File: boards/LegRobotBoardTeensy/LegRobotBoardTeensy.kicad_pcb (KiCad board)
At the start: 2 copper layers, 142.8 x 110.9 mm, 164 parts, among them J1 IDC, J10 IDC, J11 IDC, J12 IDC, J13 IDC, J14 IDC, J15 IDC, J16 IDC, J2 B3B-XH-A, J3 B3B-XH-A, J4 B3B-XH-A, J5 B3B-XH-A, J6 IDC, J7 IDC, J8 IDC, J9 IDC, Q1 AO3400A, Q10 AO3400A, Q11 AO3400A, Q12 AO3400A, Q13 AO3400A, Q14 AO3400A, Q15 AO3400A, Q16 AO3400A, Q17 AO3400A, Q18 AO3400A, Q19 AO3400A, Q2 AO3400A, Q20 AO3400A, Q21 AO3400A, Q22 AO3400A, Q23 AO3400A, Q24 AO3400A, Q3 AO3400A, Q4 AO3400A, Q5 AO3400A, Q6 AO3400A, Q7 AO3400A, Q8 AO3400A, Q9 AO3400A, U1 Teensy4.0, U2 TLC555CDR, U3 SN74HC08DR, U4 SN74HC08DR, U5 PCA9685PW_118, U6 SN74HC08DR, U7 SN74HC08DR, U8 BNO055

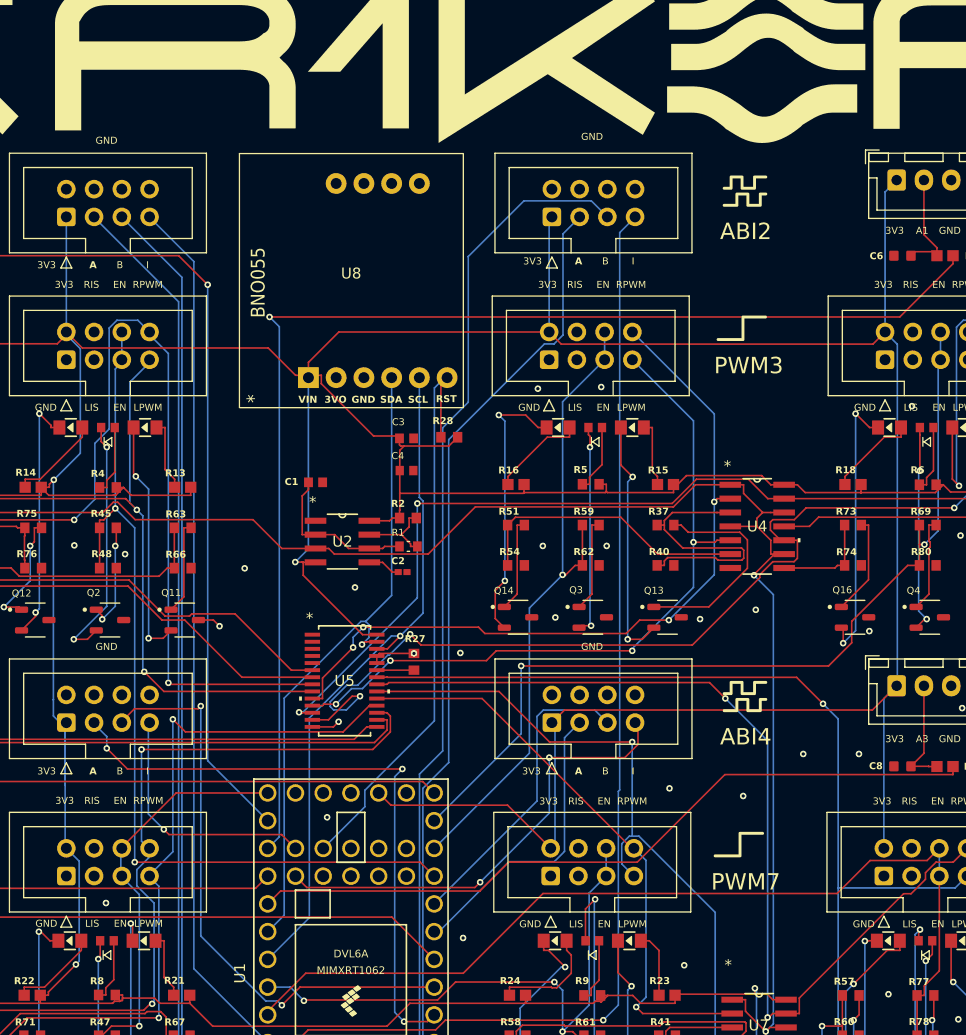
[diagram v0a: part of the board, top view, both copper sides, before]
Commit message: Re-routing leg board after rotating IMU
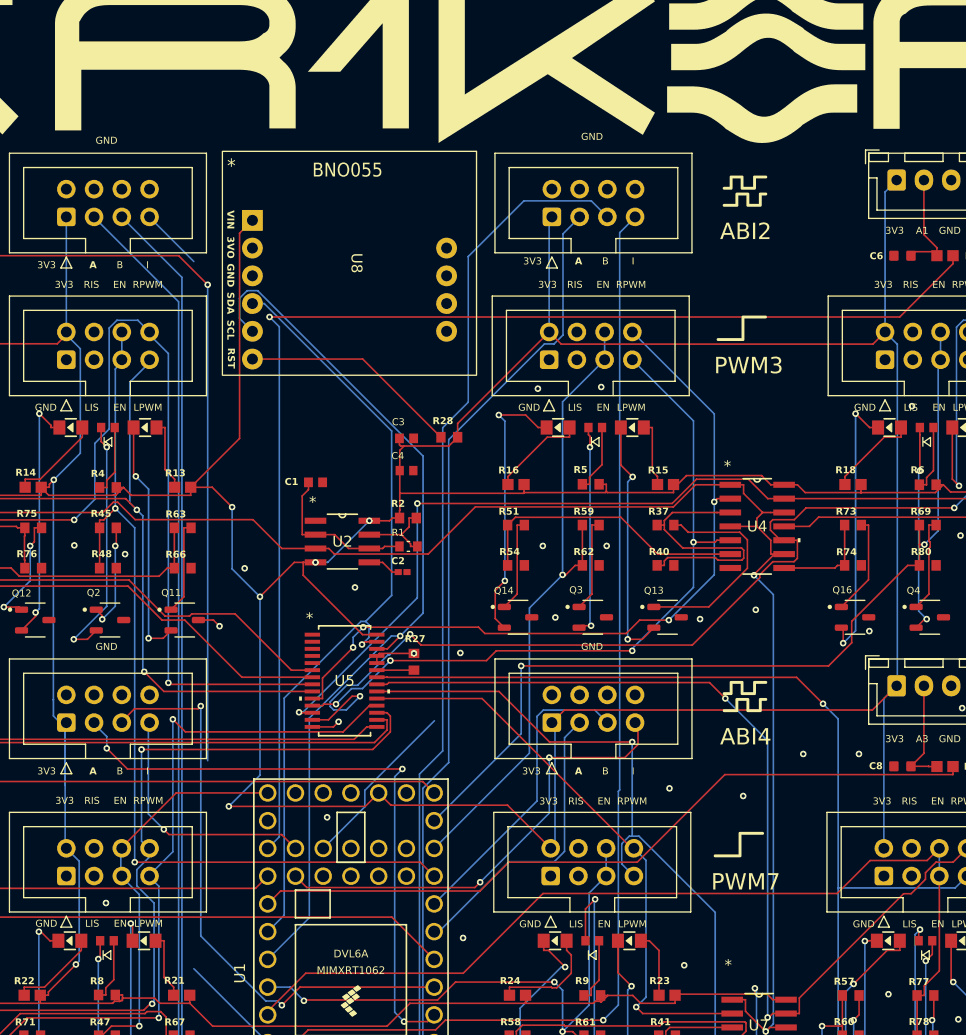
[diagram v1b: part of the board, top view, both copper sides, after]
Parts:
- moved U8 1.45 mm to (124.0, 47.8), turned to -90 degrees
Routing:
- net ENCODER1_I: track 80.1 -> 15.3 mm
- net +3.3V: track 704.4 -> 726.6 mm, vias 5 -> 9
- net SCL: track 62.6 -> 82.0 mm
- net RST: track 53.7 -> 36.1 mm
- net SDA: track 59.9 -> 72.4 mm
- net A0: track 88.5 -> 80.7 mm
- net (no net): vias 3 -> 2

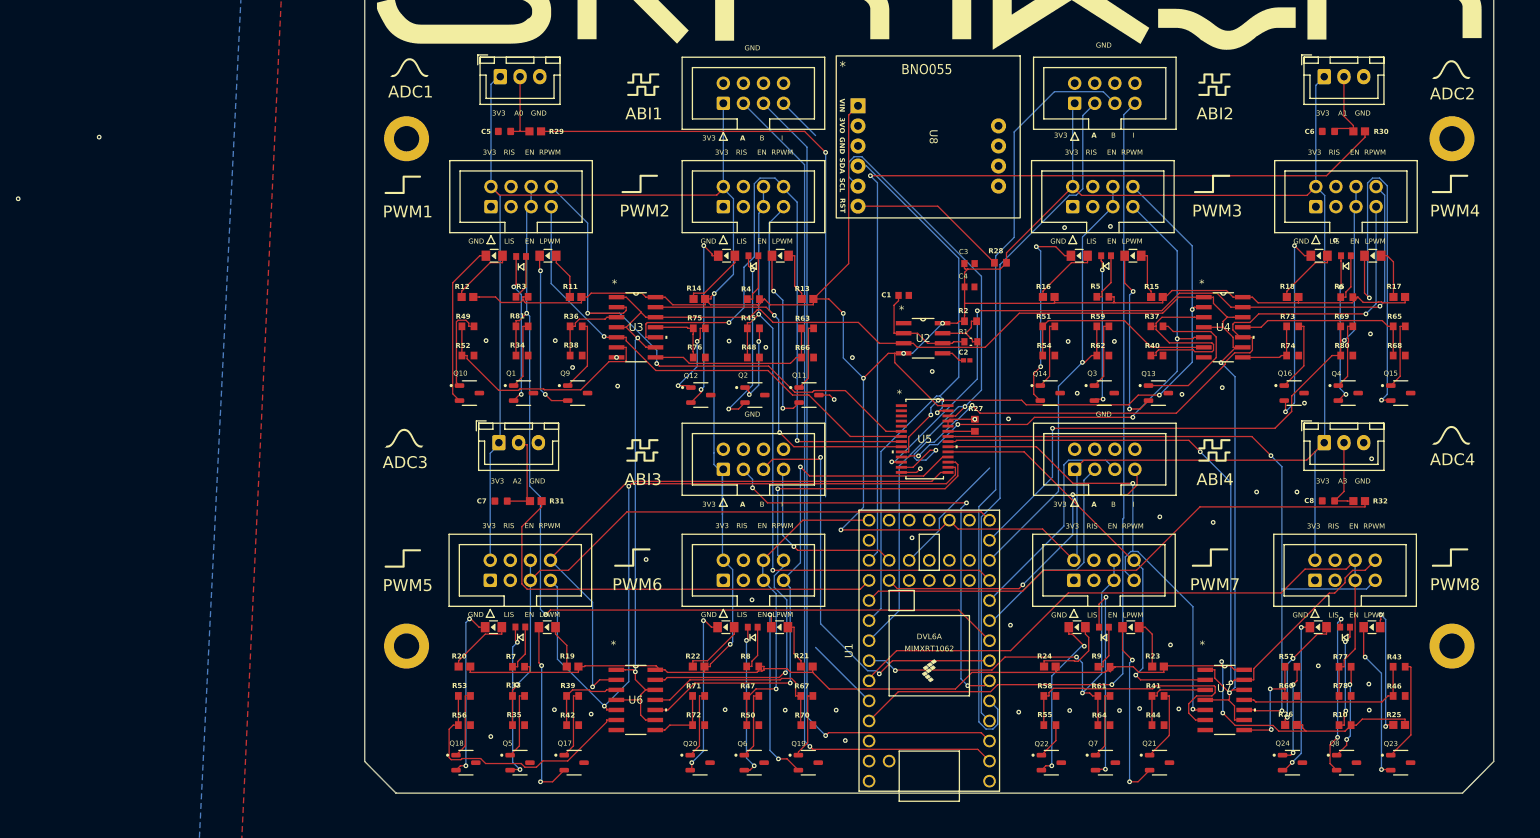
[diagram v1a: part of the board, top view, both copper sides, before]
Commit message: Add LED number displays to legs board and re-finalize
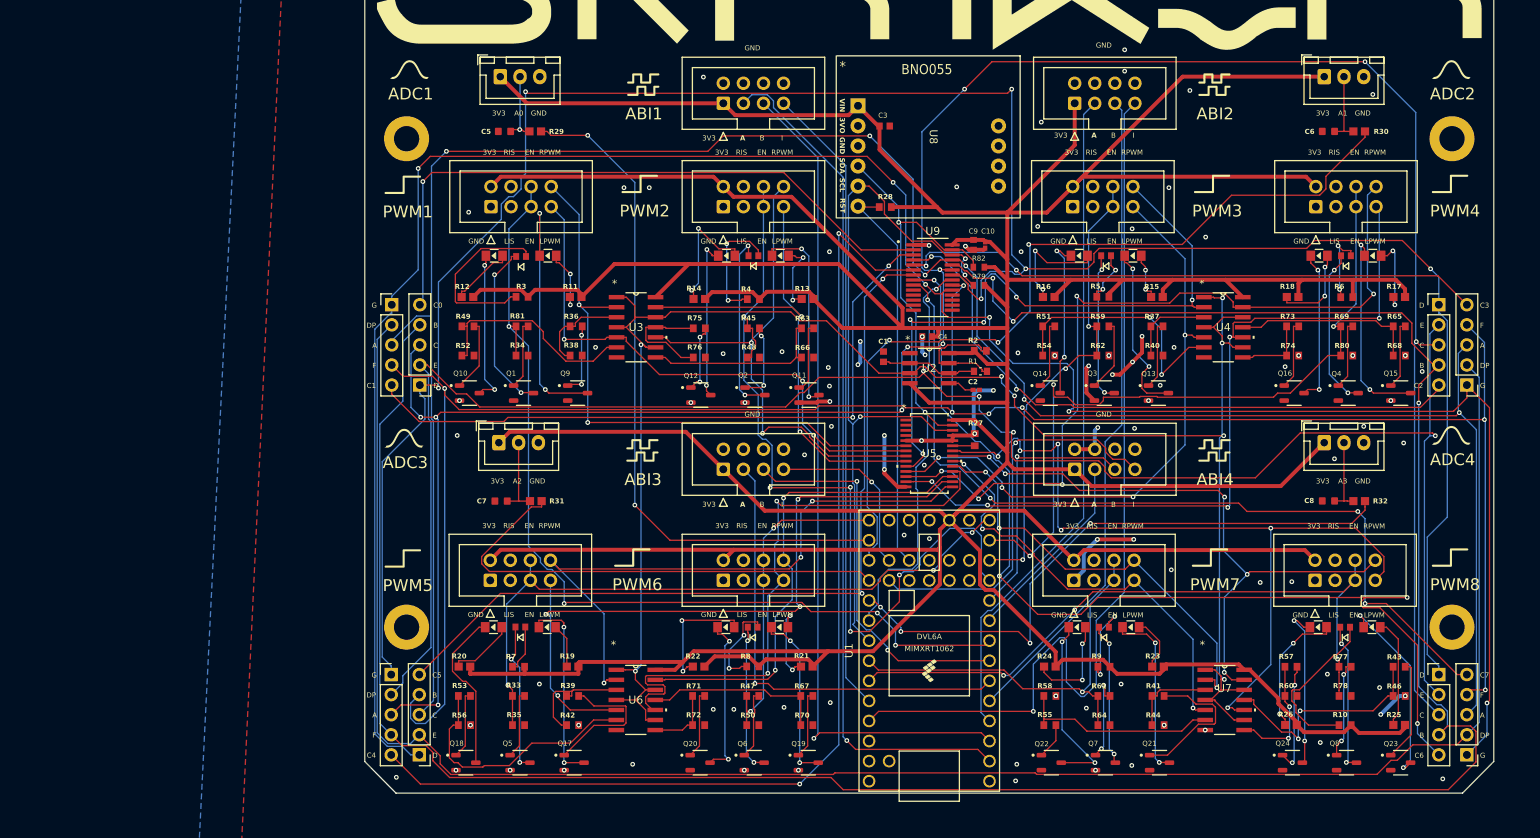
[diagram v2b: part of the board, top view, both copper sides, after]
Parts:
- added C10: 10nF, C0402C103J4RACTU:C0402C103J4RACTU, F.Cu at (131.1, 61.5)
- added C9: 100nF, CC0603KRX7R9BB104:CC0603KRX7R9BB104, F.Cu at (129.6, 61.5)
- added J17: Conn_01x05, Connector_PinHeader_2.54mm:PinHeader_1x05_P2.54mm_Vertical, F.Cu at (56.0, 69.1)
- added J18: Conn_01x05, Connector_PinHeader_2.54mm:PinHeader_1x05_P2.54mm_Vertical, F.Cu at (59.6, 79.2)
- added J19: Conn_01x05, Connector_PinHeader_2.54mm:PinHeader_1x05_P2.54mm_Vertical, F.Cu at (188.5, 69.1)
- added J20: Conn_01x05, Connector_PinHeader_2.54mm:PinHeader_1x05_P2.54mm_Vertical, F.Cu at (192.1, 79.2)
- added J21: Conn_01x05, Connector_PinHeader_2.54mm:PinHeader_1x05_P2.54mm_Vertical, F.Cu at (56.0, 115.8)
- added J22: Conn_01x05, Connector_PinHeader_2.54mm:PinHeader_1x05_P2.54mm_Vertical, F.Cu at (59.5, 126.0)
- added J23: Conn_01x05, Connector_PinHeader_2.54mm:PinHeader_1x05_P2.54mm_Vertical, F.Cu at (188.5, 115.8)
- added J24: Conn_01x05, Connector_PinHeader_2.54mm:PinHeader_1x05_P2.54mm_Vertical, F.Cu at (192.1, 126.0)
- added R79: 4.7K, CR0603-FX-4701ELF:CR0603-FX-4701ELF, F.Cu at (130.3, 66.6)
- added R82: 4.7K, CR0603-FX-4701ELF:CR0603-FX-4701ELF, F.Cu at (130.3, 64.3)
- added U9: HT16K33A-28SSOP, LCDDriver:HT16K33A-28SSOP, F.Cu at (124.5, 65.6)
- moved C3 20.4 mm to (118.4, 46.5)
- moved R28 16.2 mm to (118.5, 56.7)
- moved C4 8.26 mm to (123.8, 73.1), turned to 180 degrees
- moved C1 8.17 mm to (118.2, 75.6), turned to 90 degrees
- moved R2 3.94 mm to (130.5, 74.9)
- moved R1 3.93 mm to (130.5, 77.5)
- moved C2 3.93 mm to (130.0, 79.8)
- moved U2 3.86 mm to (124.0, 77.1)
- moved MH3 2.40 mm to (57.9, 109.8)
- moved MH4 2.40 mm to (190.2, 109.8)
- moved U5 1.91 mm to (124.0, 87.9)
- moved R27 1.83 mm to (129.8, 86.1)
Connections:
- Q1 pad 2: Net-(D1-K) -> GND
- Q1 pad 3: GND -> Net-(D1-K)
- Q10 pad 2: Net-(D10-K) -> GND
- Q10 pad 3: GND -> Net-(D10-K)
- Q11 pad 2: Net-(D11-K) -> GND
- Q11 pad 3: GND -> Net-(D11-K)
- Q12 pad 2: Net-(D12-K) -> GND
- Q12 pad 3: GND -> Net-(D12-K)
- Q13 pad 2: Net-(D13-K) -> GND
- Q13 pad 3: GND -> Net-(D13-K)
- Q14 pad 2: Net-(D14-K) -> GND
- Q14 pad 3: GND -> Net-(D14-K)
- Q15 pad 2: Net-(D15-K) -> GND
- Q15 pad 3: GND -> Net-(D15-K)
- Q16 pad 2: Net-(D16-K) -> GND
- Q16 pad 3: GND -> Net-(D16-K)
- Q17 pad 2: Net-(D17-K) -> GND
- Q17 pad 3: GND -> Net-(D17-K)
- Q18 pad 2: Net-(D18-K) -> GND
- Q18 pad 3: GND -> Net-(D18-K)
- Q19 pad 2: Net-(D19-K) -> GND
- Q19 pad 3: GND -> Net-(D19-K)
- Q2 pad 2: Net-(D2-K) -> GND
- Q2 pad 3: GND -> Net-(D2-K)
- Q20 pad 2: Net-(D20-K) -> GND
- Q20 pad 3: GND -> Net-(D20-K)
- Q21 pad 2: Net-(D21-K) -> GND
- Q21 pad 3: GND -> Net-(D21-K)
- Q22 pad 2: Net-(D22-K) -> GND
- Q22 pad 3: GND -> Net-(D22-K)
- Q23 pad 2: Net-(D23-K) -> GND
- Q23 pad 3: GND -> Net-(D23-K)
- Q24 pad 2: Net-(D24-K) -> GND
- Q24 pad 3: GND -> Net-(D24-K)
- Q3 pad 2: Net-(D3-K) -> GND
- Q3 pad 3: GND -> Net-(D3-K)
- Q4 pad 2: Net-(D4-K) -> GND
- Q4 pad 3: GND -> Net-(D4-K)
- Q5 pad 2: Net-(D5-K) -> GND
- Q5 pad 3: GND -> Net-(D5-K)
- Q6 pad 2: Net-(D6-K) -> GND
- Q6 pad 3: GND -> Net-(D6-K)
- Q7 pad 2: Net-(D7-K) -> GND
- Q7 pad 3: GND -> Net-(D7-K)
- Q8 pad 2: Net-(D8-K) -> GND
- Q8 pad 3: GND -> Net-(D8-K)
- Q9 pad 2: Net-(D9-K) -> GND
- Q9 pad 3: GND -> Net-(D9-K)
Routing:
- net DIGIT_B: track 0.00 -> 327.1 mm, vias 0 -> 3
- net DIGIT_C: track 0.00 -> 307.5 mm, vias 0 -> 10
- net DIGIT_D: track 0.00 -> 292.8 mm, vias 0 -> 6
- net DIGIT_G: track 0.00 -> 292.5 mm, vias 0 -> 6
- net DIGIT_A: track 0.00 -> 285.6 mm, vias 0 -> 6
- net DIGIT_F: track 0.00 -> 259.5 mm, vias 0 -> 7
- net DIGIT_E: track 0.00 -> 252.0 mm, vias 0 -> 5
- net DIGIT_DP: track 0.00 -> 244.3 mm
- net +3.3V: track 726.6 -> 895.5 mm, vias 9 -> 0
- net COM4: track 0.00 -> 136.3 mm, vias 0 -> 2
- net COM6: track 0.00 -> 130.5 mm, vias 0 -> 4
- net COM7: track 0.00 -> 108.6 mm, vias 0 -> 4
- net COM5: track 0.00 -> 105.3 mm, vias 0 -> 2
- net COM1: track 0.00 -> 85.9 mm, vias 0 -> 2
- net COM0: track 0.00 -> 82.3 mm, vias 0 -> 1
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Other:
- board text added: "C"
- board text added: "C0"
- board text added: "C1"
- board text added: "C2"
- board text added: "C3"
- board text added: "C4"
- board text added: "C5"
- board text added: "C6"
- board text added: "C7"
- board text added: "D"
- board text added: "DP"
- board text added: "E"
- board text added: "F"
- board text added: "G"

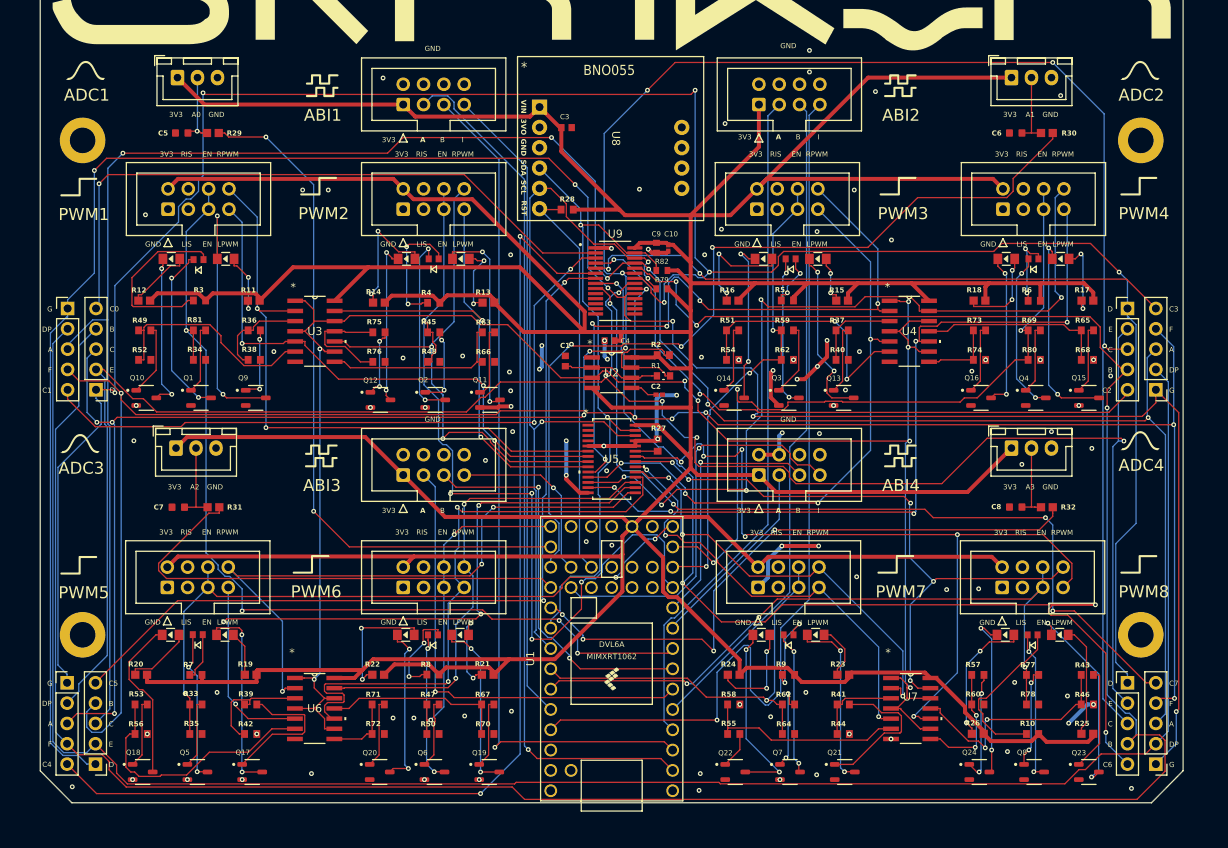
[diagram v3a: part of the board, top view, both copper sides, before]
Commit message: Re-order leg board with different LED control chip
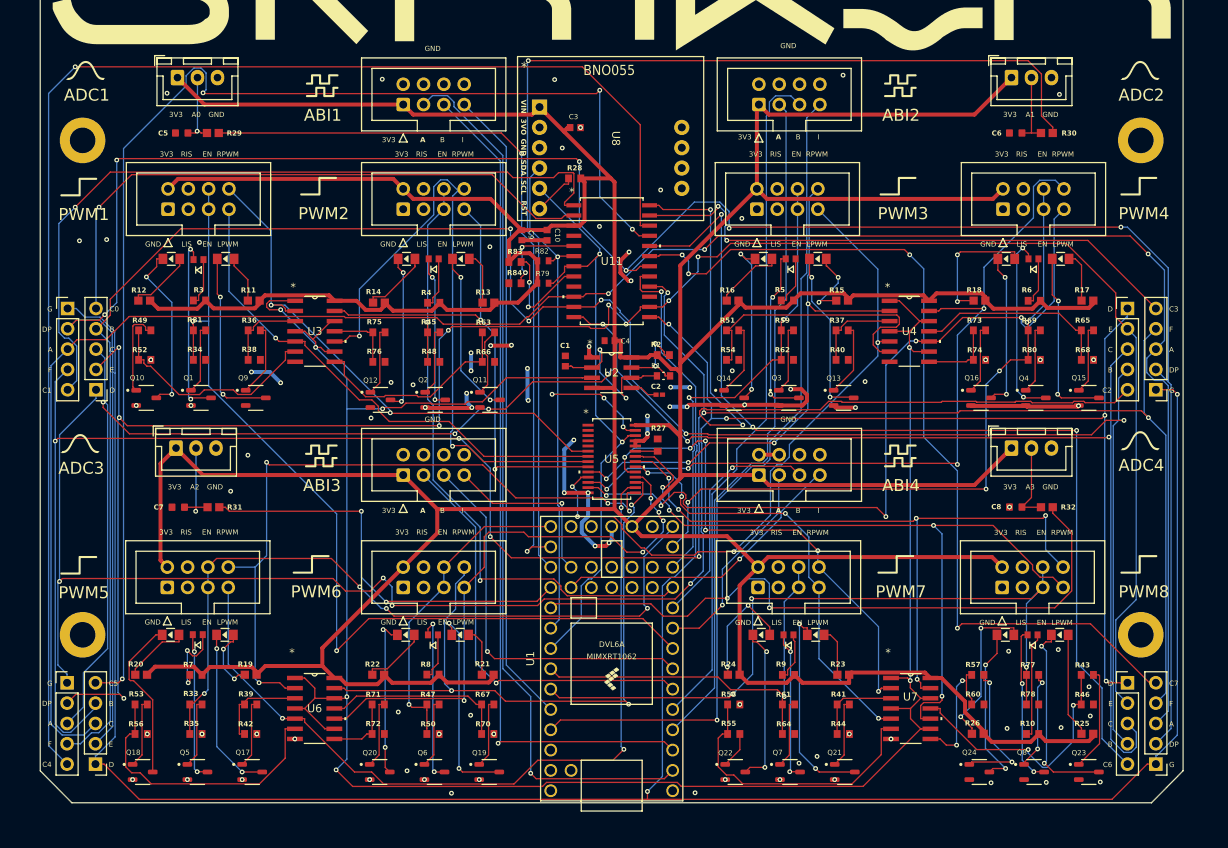
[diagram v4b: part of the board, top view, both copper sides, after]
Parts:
- removed U9: HT16K33A-28SSOP, LCDDriver:HT16K33A-28SSOP
- added R83: 10K, CRCW060310K0FKEA:CRCW060310K0FKEA, F.Cu at (111.9, 63.2)
- added R84: 20K, CRCW060310K0FKEA:CRCW060310K0FKEA, F.Cu at (111.9, 65.9)
- added U11: IS31FL3739-GRLS4-TR, IS31FL3730-QFLS2-TR:IS31FL3730-QFLS2-TR, F.Cu at (124.0, 63.1)
- C10: value 10nF -> 1uF; footprint C0402C103J4RACTU:C0402C103J4RACTU -> CC0603JRX7R7BB105:CC0603JRX7R7BB105
- moved C9 16.9 mm to (112.8, 59.9)
- moved C10 15.2 mm to (116.0, 59.9)
- moved R82 14.9 mm to (115.4, 63.1), turned to 0 degrees
- moved R79 14.9 mm to (115.4, 65.9), turned to 0 degrees
- moved R28 4.01 mm to (119.4, 52.8)
- moved C3 1.10 mm to (119.5, 46.5)
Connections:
- R28 pad 1: RST -> Net-(R28-Pad1)
- U1 pad 37: RST -> unconnected-(U1-26_A12_MOSI1-Pad37)
- U8 pad RST: RST -> Net-(R28-Pad1)
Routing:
- net +3.3V: track 895.5 -> 752.4 mm
- net DIGIT_B: track 327.1 -> 263.3 mm, vias 3 -> 5
- net DIGIT_DP: track 244.3 -> 300.2 mm, vias 0 -> 6
- net DIGIT_C: track 307.5 -> 252.8 mm, vias 10 -> 7
- net COM5: track 105.3 -> 159.4 mm, vias 2 -> 4
- net RST: track 50.2 -> 0.00 mm
- net BLINK: track 230.1 -> 275.1 mm, vias 8 -> 7
- net COM4: track 136.3 -> 176.9 mm, vias 2 -> 1
- net DIGIT_D: track 292.8 -> 262.1 mm, vias 6 -> 8
- net DIGIT_G: track 292.5 -> 322.4 mm, vias 6 -> 3
- net A1: track 108.1 -> 137.4 mm, vias 3 -> 1
- net DIGIT_F: track 259.5 -> 287.4 mm
- net GND: track 72.1 -> 99.5 mm, vias 97 -> 91
- net DIGIT_A: track 285.6 -> 259.9 mm, vias 6 -> 3
- net PWMEN2: track 107.4 -> 83.2 mm, vias 5 -> 2
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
